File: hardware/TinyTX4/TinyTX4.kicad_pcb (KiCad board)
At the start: 2 copper layers, 25 x 43.9 mm, 14 parts, among them J1 Conn_01x03_Male, J2 Conn_01x08_Female, J3 Conn_01x08_Female, J4 Conn_01x08_Female, U1 ATtiny1614-SS, U2 RFM69HW, U3 MCP1703A-3302_SOT23

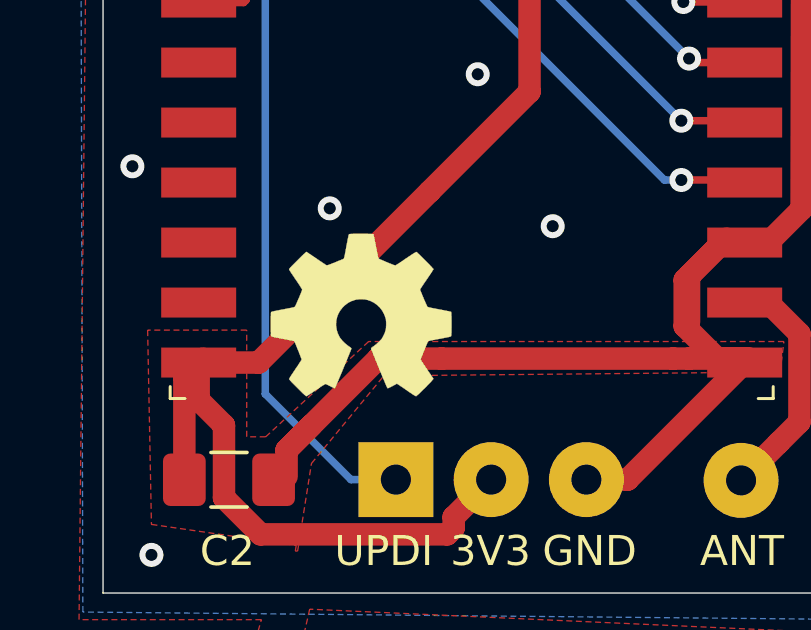
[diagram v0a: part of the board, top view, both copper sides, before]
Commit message: Add 3d graphic
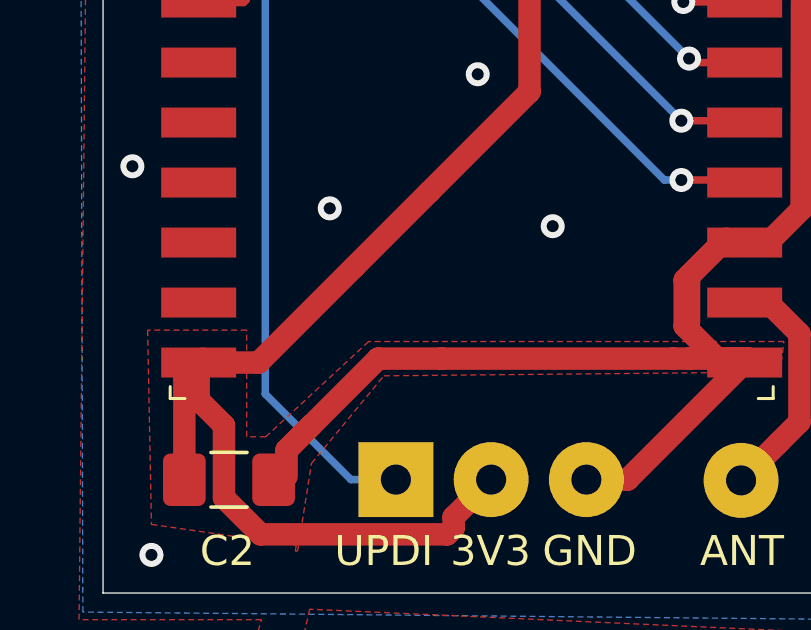
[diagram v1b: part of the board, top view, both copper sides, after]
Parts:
- G***: moved to B.Cu
- moved G*** 4.39 mm to (26.5, 46.7), turned to 180 degrees
